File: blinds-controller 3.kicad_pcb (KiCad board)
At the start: 2 copper layers, 50 x 70 mm, 13 parts, among them J1 Jack-DC, J2 Stepper Motor, J3 DC Check, J4 JTAG, SW1 BOOT, U1 MPM3610AGQV-P, U2 ESP32-S2-WROOM, U3 ULN2003A

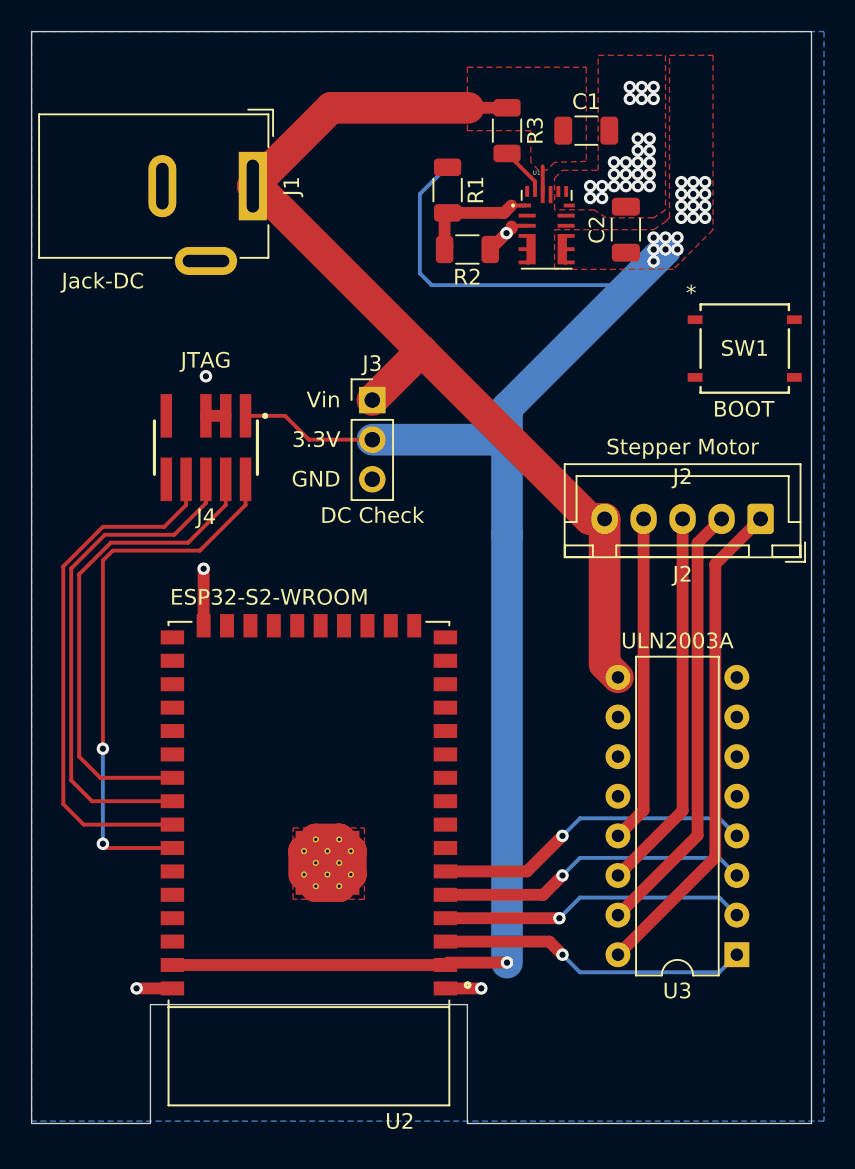
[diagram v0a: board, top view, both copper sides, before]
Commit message: Added switch symbol to library
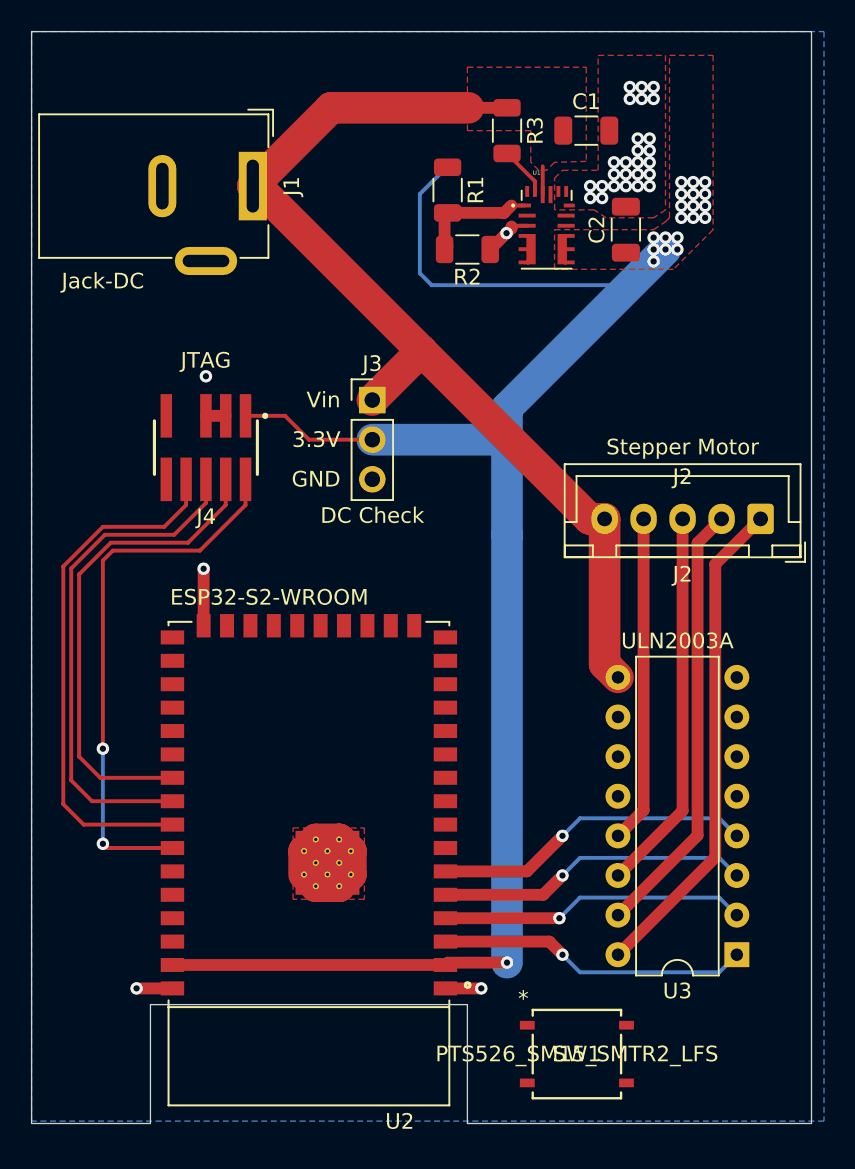
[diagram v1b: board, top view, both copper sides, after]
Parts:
- SW1: value BOOT -> PTS526_SM15_SMTR2_LFS
- moved SW1 46.5 mm to (88.3, 84.6)
